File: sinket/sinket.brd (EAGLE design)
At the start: 36 x 36 mm, 25 parts, among them IC1 ATTINY85-20PU, IC2 TS2940CP50S

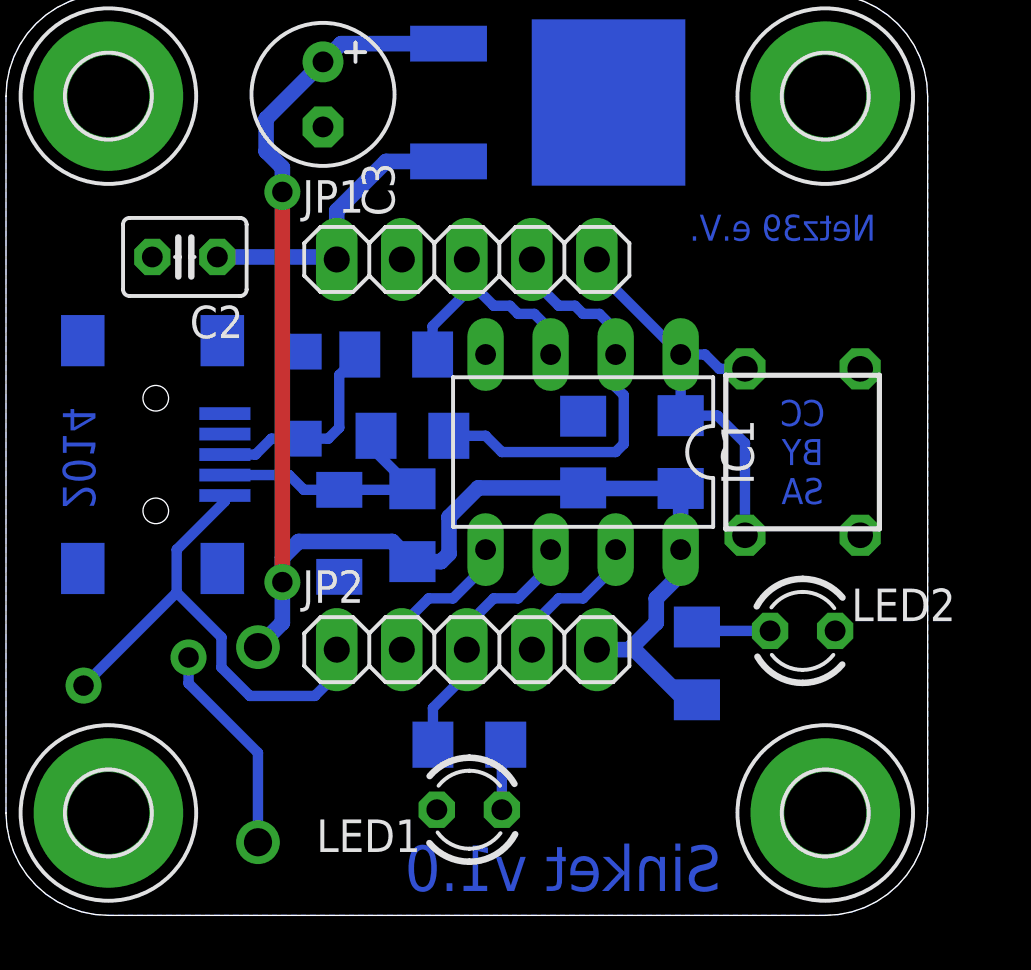
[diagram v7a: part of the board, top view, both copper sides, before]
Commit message: LED package changed, Schraubklemme added, parts moved
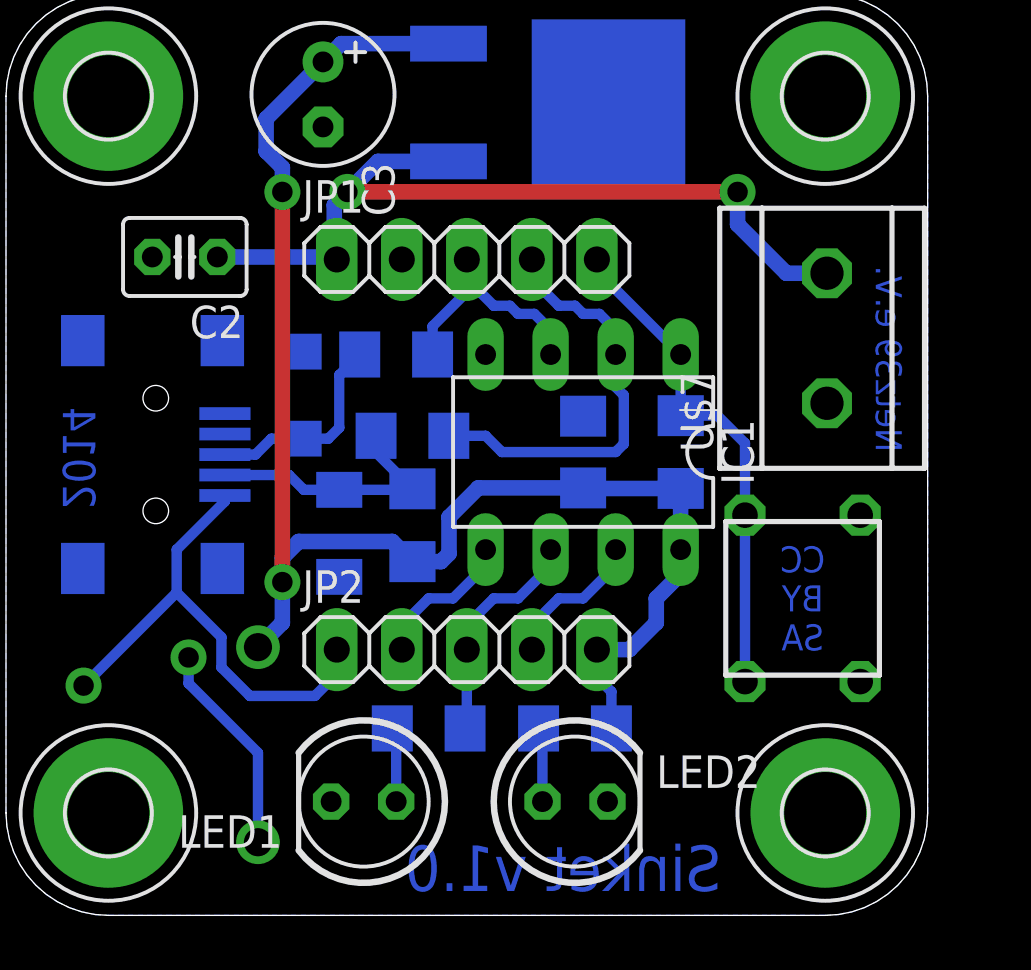
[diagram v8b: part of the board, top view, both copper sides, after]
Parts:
- added U$7: RIACON_101_2, n39:RIACON_101_2
- F1: value (none) -> 500mA
- LED1, LED2: device led:LED3MM -> led:LED5MM
- moved LED2 11.1 mm to (22.2, 4.45)
- moved U$6 5.71 mm to (31.1, 12.4)
- moved R5 5.40 mm to (22.2, 7.30), turned to 0 degrees
- moved LED1 4.14 mm to (14.0, 4.45)
- moved R2 1.71 mm to (16.5, 7.30), turned to 0 degrees
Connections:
- net GND: now also U$7.1
- net VBAT: now also U$7.2
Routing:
- net VBAT: track 11.8 -> 32.7 mm, vias 0 -> 2
- net !RESET: track 16.8 -> 19.7 mm
- net B1: track 10.1 -> 8.93 mm
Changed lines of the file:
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@@
 <setting verticaltext="up"/>
 </settings>
-<grid distance="12.5" unitdist="mil" unit="mil" style="dots" multiple="1" display="no" altdistance="25" altunitdist="mil" altunit="mil"/>
+<grid distance="12.5" unitdist="mil" unit="mil" style="dots" multiple="1" display="yes" altdistance="25" altunitdist="mil" altunit="mil"/>
 <layers>
 <layer number="1" name="Top" color="4" fill="1" visible="yes" active="yes"/>
@@
 <wire x1="0" y1="32" x2="0" y2="4" width="0" layer="20"/>
 <wire x1="0" y1="4" x2="4" y2="0" width="0" layer="20" curve="90"/>
-<circle x="23.495" y="5.715" radius="2" width="0" layer="42"/>
+<circle x="29.5275" y="22.5425" radius="1.5" width="0" layer="42"/>
 <text x="27.94" y="0.9525" size="1.778" layer="16" font="vector" ratio="13" rot="MR0">Sinket v1.0</text>
 <text x="2.2225" y="15.875" size="1.27" layer="16" font="vector" ratio="13" rot="MR90">2014</text>
-<text x="31.115" y="18.0975" size="1.016" layer="16" font="vector" ratio="13" rot="MR0" align="center">CC
+<text x="31.115" y="12.3825" size="1.016" layer="16" font="vector" ratio="13" rot="MR0" align="center">CC
 BY
 SA</text>
-<text x="33.9725" y="26.3525" size="1.016" layer="16" font="vector" ratio="13" rot="MR0">Netz39 e.V.</text>
+<text x="33.9725" y="18.0975" size="1.016" layer="16" font="vector" ratio="13" rot="MR90">Netz39 e.V.</text>
+<rectangle x1="33.655" y1="17.78" x2="34.925" y2="27.305" layer="42"/>
 </plain>
 <attributes>
@@
 <element name="U$4" library="holes" package="3,2-PAD" value="" x="32" y="32"/>
 <element name="U$5" library="holes" package="3,2-PAD" value="" x="4" y="32"/>
-<element name="U$6" library="n39" package="JTP-1130" value="JTP-1130C" x="31.115" y="18.0975" rot="R90">
-<attribute name="REICHELT" value="TASTER 9305" x="31.115" y="18.0975" size="1.778" layer="27" rot="R90" display="off"/>
+<element name="U$6" library="n39" package="JTP-1130" value="JTP-1130C" x="31.115" y="12.3825" rot="R90">
+<attribute name="REICHELT" value="TASTER 9305" x="31.115" y="12.3825" size="1.778" layer="27" rot="R90" display="off"/>
 </element>
 <element name="R1" library="rcl" package="R1206" value="10k" x="26.3525" y="18.0975" rot="MR270"/>
-<element name="R2" library="rcl" package="R1206" value="1k5" x="18.0975" y="6.6675" rot="MR180"/>
+<element name="R2" library="rcl" package="R1206" value="1k5" x="16.51" y="7.3025" rot="MR0"/>
 <element name="R3" library="rcl" package="R1206" value="68" x="15.875" y="18.7325" rot="MR0"/>
 <element name="R4" library="rcl" package="R1206" value="68" x="15.24" y="21.9075" rot="MR0"/>
-<element name="R5" library="rcl" package="R1206" value="1k5" x="26.9875" y="9.8425" rot="MR90"/>
+<element name="R5" library="rcl" package="R1206" value="1k5" x="22.225" y="7.3025" rot="MR0"/>
 <element name="R6" library="rcl" package="R1206" value="1k5" x="15.875" y="15.24" rot="MR90"/>
 <element name="D1" library="diode" package="SOD80C" value="3V6" x="13.0175" y="14.9225" rot="MR270"/>
 <element name="D2" library="diode" package="SOD80C" value="3V6" x="11.43" y="20.32" rot="MR90"/>
-<element name="LED1" library="led" package="LED3MM" value="red" x="18.0975" y="4.1275" rot="R180"/>
-<element name="LED2" library="led" package="LED3MM" value="green" x="31.115" y="11.1125"/>
+<element name="LED1" library="led" package="LED5MM" value="red" x="13.97" y="4.445" rot="R180"/>
+<element name="LED2" library="led" package="LED5MM" value="green" x="22.225" y="4.445"/>
 <element name="C1" library="rcl" package="C1206" value="100n" x="22.5425" y="18.0975" rot="MR90"/>
 <element name="D3" library="diode" package="DO41-7.6" value="1N5817-B" x="9.8425" y="6.6675" rot="MR270"/>
@@
 <element name="C2" library="rcl" package="C025-030X050" value="470n" x="6.985" y="25.7175" rot="R180"/>
 <element name="C3" library="rcl" package="E2,5-6" value="47u" x="12.3825" y="32.0675" rot="R270"/>
-<element name="F1" library="n39" package="LP60-050" value="" x="5.08" y="9.525" rot="MR180"/>
+<element name="F1" library="n39" package="LP60-050" value="500mA" x="5.08" y="9.525" rot="MR180"/>
+<element name="U$7" library="n39" package="RIACON_101_2" value="RIACON_101_2" x="32.0675" y="22.5425" rot="R90">
+<attribute name="REICHELT" value="AKL 101-02" x="32.0675" y="22.5425" size="1.778" layer="27" rot="R90" display="off"/>
+</element>
 </elements>
 <signals>
@@
 <wire x1="26.3525" y1="13.335" x2="25.4" y2="12.3825" width="0.6096" layer="16"/>
 <wire x1="25.4" y1="12.3825" x2="25.4" y2="11.43" width="0.6096" layer="16"/>
-<wire x1="25.4" y1="11.43" x2="24.4475" y2="10.4775" width="0.6096" layer="16"/>
-<wire x1="24.4475" y1="10.4775" x2="24.35" y2="10.38" width="0.6096" layer="16"/>
+<wire x1="25.4" y1="11.43" x2="24.35" y2="10.38" width="0.6096" layer="16"/>
 <wire x1="23.08" y1="10.38" x2="24.35" y2="10.38" width="0.6096" layer="16"/>
-<wire x1="26.9875" y1="8.4205" x2="26.5045" y2="8.4205" width="0.6096" layer="16"/>
-<wire x1="26.5045" y1="8.4205" x2="24.4475" y2="10.4775" width="0.6096" layer="16"/>
+<wire x1="23.647" y1="7.3025" x2="23.647" y2="8.738" width="0.4064" layer="16"/>
+<wire x1="23.08" y1="10.38" x2="23.08" y2="9.305" width="0.4064" layer="16"/>
+<wire x1="23.08" y1="9.305" x2="23.647" y2="8.738" width="0.4064" layer="16"/>
 </signal>
 <signal name="VBUS" class="1">
@@
 <contactref element="C3" pad="-"/>
 <contactref element="IC2" pad="2"/>
+<contactref element="U$7" pad="1"/>
 </signal>
 <signal name="VBAT" class="1">
@@
 <wire x1="8.255" y1="25.7175" x2="12.8225" y2="25.7175" width="0.6096" layer="16"/>
 <wire x1="12.8225" y1="25.7175" x2="12.92" y2="25.62" width="0.6096" layer="16"/>
-<wire x1="12.92" y1="25.62" x2="12.92" y2="27.525" width="0.6096" layer="16"/>
-<wire x1="17.285" y1="29.45" x2="14.845" y2="29.45" width="0.6096" layer="16"/>
-<wire x1="14.845" y1="29.45" x2="12.92" y2="27.525" width="0.6096" layer="16"/>
+<contactref element="U$7" pad="2"/>
+<via x="28.575" y="28.2575" extent="1-16" drill="0.8" shape="square"/>
+<wire x1="28.575" y1="28.2575" x2="13.335" y2="28.2575" width="0.6096" layer="1"/>
+<via x="13.335" y="28.2575" extent="1-16" drill="0.8" shape="square"/>
+<wire x1="32.0675" y1="25.0825" x2="30.48" y2="25.0825" width="0.6096" layer="16"/>
+<wire x1="30.48" y1="25.0825" x2="28.575" y2="26.9875" width="0.6096" layer="16"/>
+<wire x1="28.575" y1="26.9875" x2="28.575" y2="28.2575" width="0.6096" layer="16"/>
+<wire x1="17.285" y1="29.45" x2="14.5275" y2="29.45" width="0.6096" layer="16"/>
+<wire x1="14.5275" y1="29.45" x2="13.335" y2="28.2575" width="0.6096" layer="16"/>
+<wire x1="12.8225" y1="25.7175" x2="12.8225" y2="27.745" width="0.6096" layer="16"/>
+<wire x1="12.8225" y1="27.745" x2="13.335" y2="28.2575" width="0.6096" layer="16"/>
 </signal>
 <signal name="N$1">
@@
 <contactref element="JP1" pad="5"/>
 <wire x1="26.3525" y1="21.9075" x2="26.3525" y2="19.5195" width="0.4064" layer="16"/>
-<wire x1="26.3525" y1="21.9075" x2="27.305" y2="21.9075" width="0.4064" layer="16"/>
-<wire x1="27.305" y1="21.9075" x2="27.865" y2="21.3475" width="0.4064" layer="16"/>
-<wire x1="28.865" y1="21.3475" x2="27.865" y2="21.3475" width="0.4064" layer="16"/>
+<wire x1="23.08" y1="25.62" x2="23.08" y2="25.18" width="0.4064" layer="16"/>
+<wire x1="23.08" y1="25.18" x2="26.3525" y2="21.9075" width="0.4064" layer="16"/>
 <wire x1="26.3525" y1="19.5195" x2="27.788" y2="19.5195" width="0.4064" layer="16"/>
 <wire x1="27.788" y1="19.5195" x2="28.865" y2="18.4425" width="0.4064" layer="16"/>
-<wire x1="28.865" y1="14.8475" x2="28.865" y2="18.4425" width="0.4064" layer="16"/>
-<wire x1="23.08" y1="25.62" x2="23.08" y2="25.18" width="0.4064" layer="16"/>
-<wire x1="23.08" y1="25.18" x2="26.3525" y2="21.9075" width="0.4064" layer="16"/>
+<wire x1="28.865" y1="18.4425" x2="28.865" y2="15.6325" width="0.4064" layer="16"/>
+<wire x1="28.865" y1="15.6325" x2="28.865" y2="9.1325" width="0.4064" layer="16"/>
 </signal>
 <signal name="B1">
@@
 <wire x1="20.0025" y1="12.3825" x2="21.2725" y2="13.6525" width="0.4064" layer="16"/>
 <wire x1="21.2725" y1="13.6525" x2="21.2725" y2="14.2875" width="0.4064" layer="16"/>
-<wire x1="18" y1="10.38" x2="18" y2="9.4275" width="0.4064" layer="16"/>
-<wire x1="18" y1="9.4275" x2="16.6755" y2="8.103" width="0.4064" layer="16"/>
-<wire x1="16.6755" y1="6.6675" x2="16.6755" y2="8.103" width="0.4064" layer="16"/>
+<wire x1="18" y1="10.38" x2="18" y2="7.3705" width="0.4064" layer="16"/>
+<wire x1="18" y1="7.3705" x2="17.932" y2="7.3025" width="0.4064" layer="16"/>
 </signal>
 <signal name="N$4">
 <contactref element="R2" pad="2"/>
 <contactref element="LED1" pad="A"/>
-<wire x1="19.5195" y1="6.6675" x2="19.3675" y2="6.6675" width="0.4064" layer="16"/>
-<wire x1="19.3675" y1="6.6675" x2="19.3675" y2="4.1275" width="0.4064" layer="16"/>
+<wire x1="15.24" y1="4.445" x2="15.24" y2="7.1505" width="0.4064" layer="16"/>
+<wire x1="15.24" y1="7.1505" x2="15.088" y2="7.3025" width="0.4064" layer="16"/>
 </signal>
 <signal name="N$5">
 <contactref element="LED2" pad="A"/>
 <contactref element="R5" pad="2"/>
-<wire x1="29.845" y1="11.1125" x2="27.1395" y2="11.1125" width="0.4064" layer="16"/>
-<wire x1="27.1395" y1="11.1125" x2="26.9875" y2="11.2645" width="0.4064" layer="16"/>
+<wire x1="20.955" y1="4.445" x2="20.955" y2="7.1505" width="0.4064" layer="16"/>
+<wire x1="20.955" y1="7.1505" x2="20.803" y2="7.3025" width="0.4064" layer="16"/>
 </signal>
 <signal name="B0">
